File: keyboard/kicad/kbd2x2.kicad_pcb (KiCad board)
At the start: 2 copper layers, 40 x 40 mm, 8 parts, among them SW1 mykbd, SW2 mykbd, SW3 mykbd, SW4 mykbd

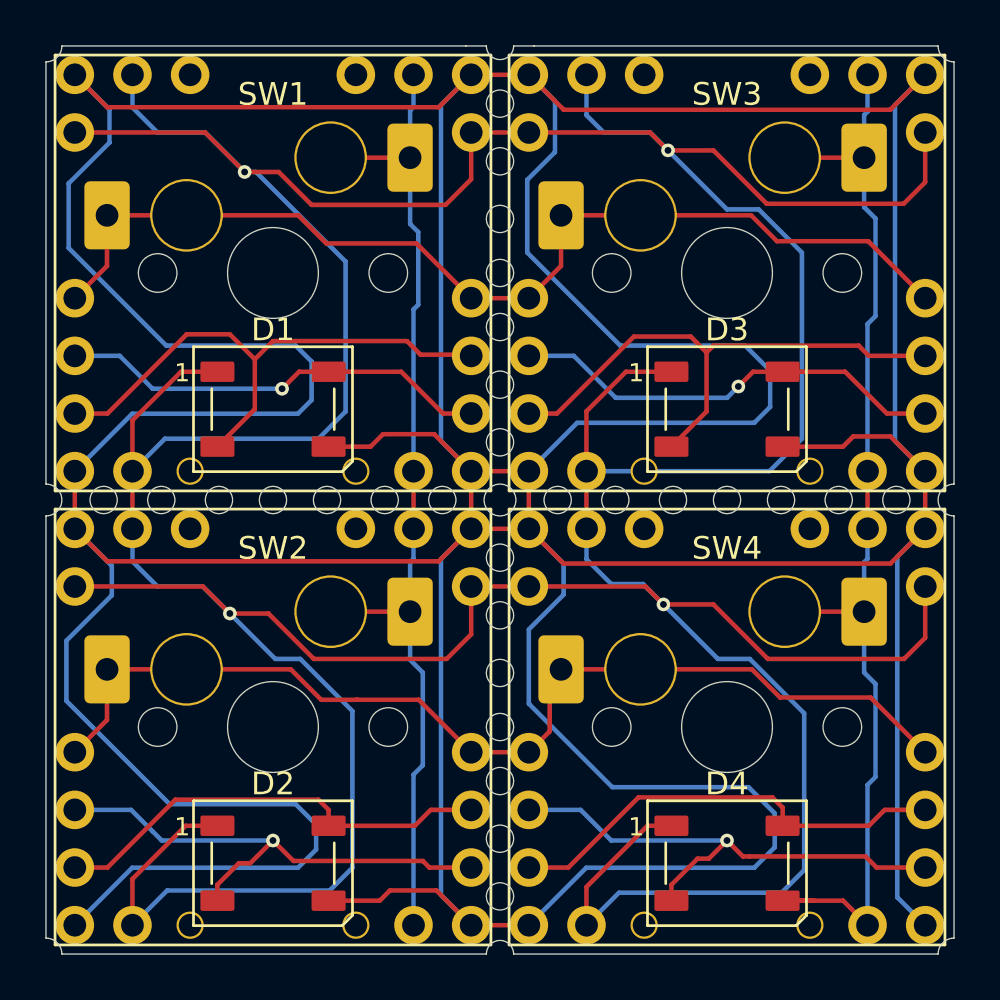
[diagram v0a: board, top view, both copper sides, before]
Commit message: keyboard pcb: bottom board(esp32s3 minimal 20mmx40mm)
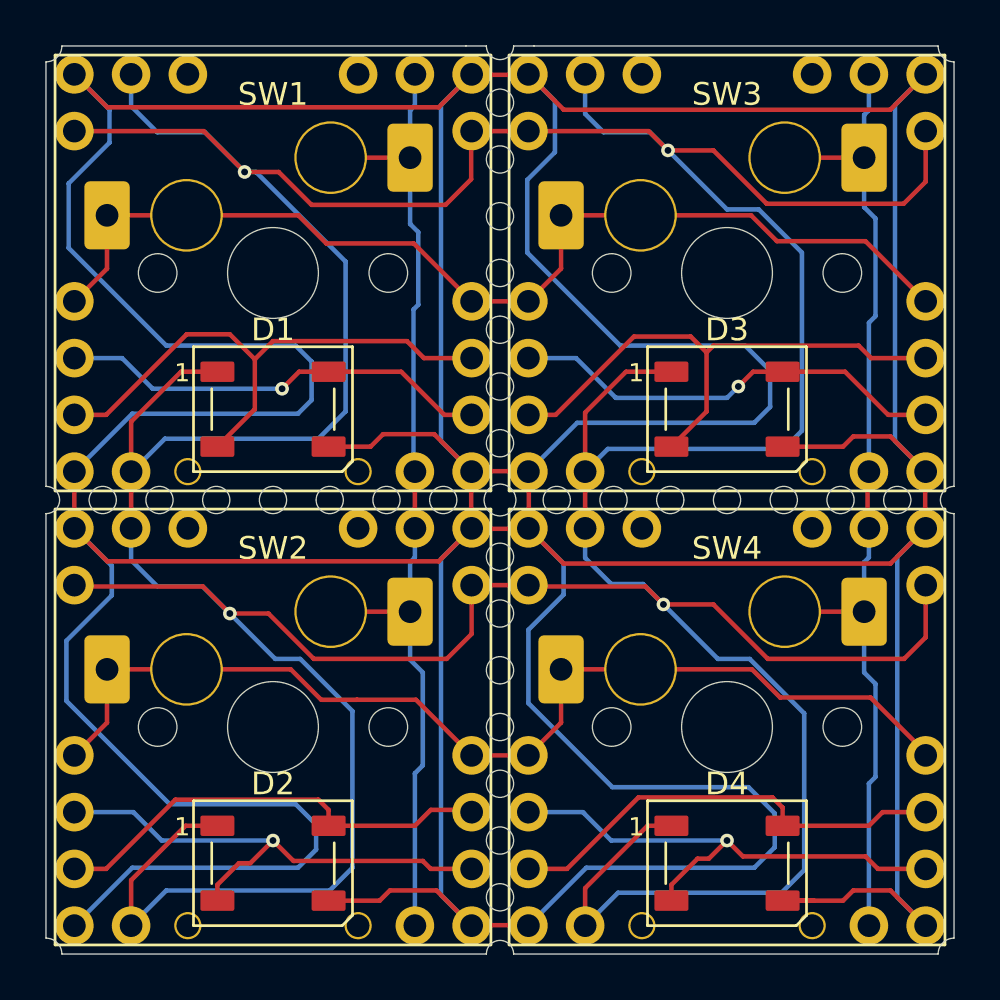
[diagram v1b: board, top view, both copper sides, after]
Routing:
- net GND: track 337.5 -> 340.5 mm
- net VCC: track 248.4 -> 249.0 mm
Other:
- outline, holes or cut-outs redrawn
